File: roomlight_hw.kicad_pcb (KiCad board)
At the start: 2 copper layers, 47.4 x 41.3 mm, 68 parts, among them J1 24V_Conn, J2 LOADs, J3 UART2, J4 DATAs, J5 Touch_SW, J6 SWD, Q1 IRF8734, Q2 IRF8734, Q3 IRF8734, U1 INA180A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

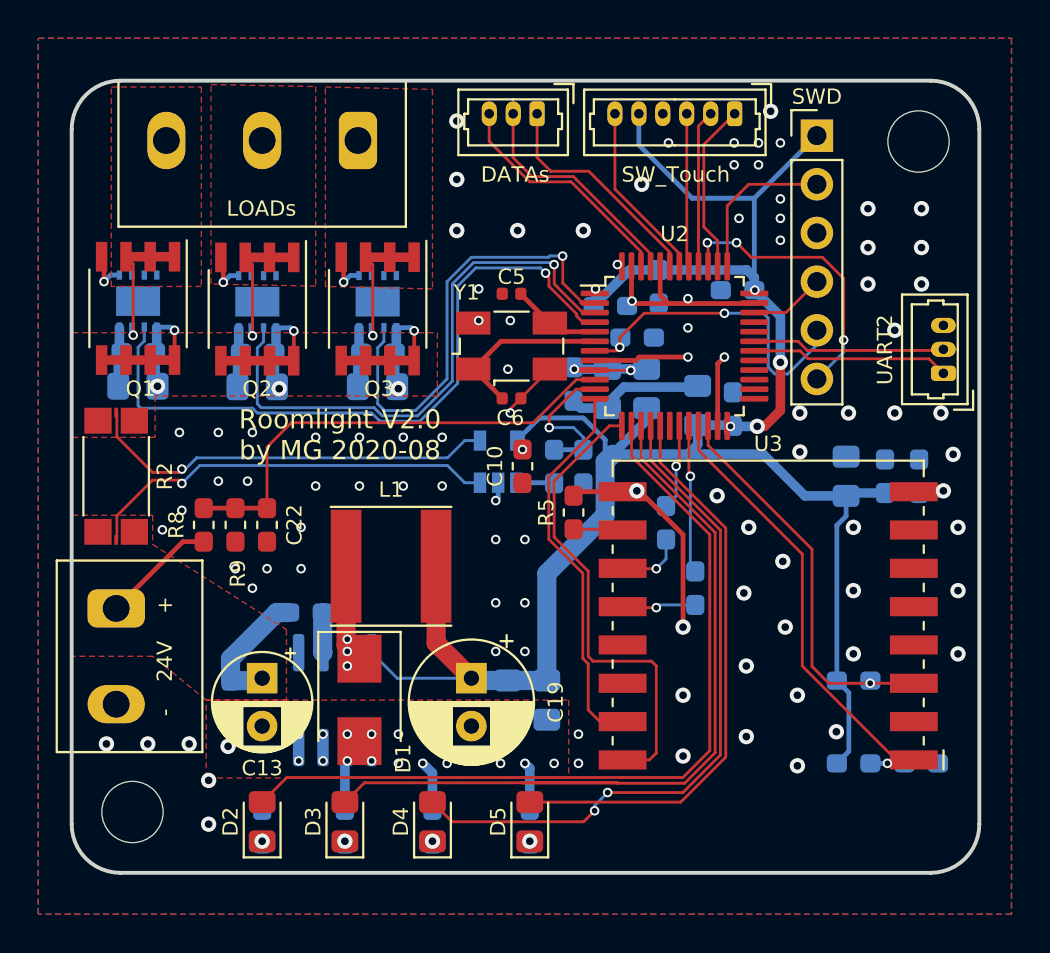
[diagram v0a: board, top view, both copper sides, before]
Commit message: Improve UART connection and a lot of ground planes
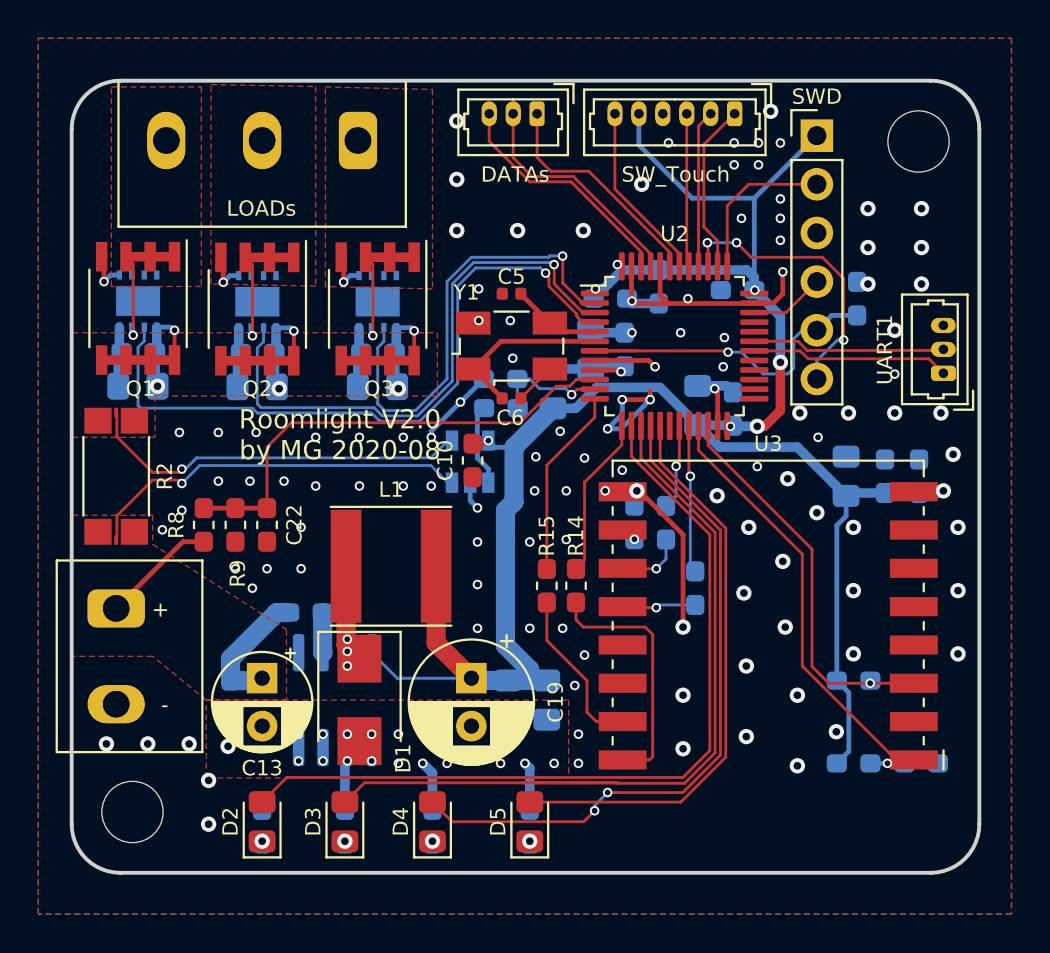
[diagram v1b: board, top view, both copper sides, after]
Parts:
- added R14: R, Resistor_SMD:R_0603_1608Metric_Pad1.05x0.95mm_HandSolder, F.Cu at (76.3, 120.0)
- added R15: R, Resistor_SMD:R_0603_1608Metric_Pad1.05x0.95mm_HandSolder, F.Cu at (74.8, 120.0)
- R5: moved to B.Cu
- moved C9 11.7 mm to (91.0, 105.0), turned to 90 degrees
- moved C3 6.29 mm to (72.4, 109.2), turned to 0 degrees
- moved FB1 4.89 mm to (75.1, 109.7)
- moved R1 4.13 mm to (72.4, 110.7), turned to 0 degrees
- moved C11 3.22 mm to (78.9, 107.7), turned to 90 degrees
- moved R5 3.22 mm to (79.4, 116.7)
- moved C10 2.62 mm to (70.9, 113.5)
- moved C12 2.22 mm to (77.1, 107.7), turned to 90 degrees
- moved U1 1.46 mm to (70.8, 113.5)
- moved C7 0.38 mm to (78.1, 105.0)
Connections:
- U3 pad 15: /UART2_TX -> Net-(R15-Pad2)
- U3 pad 16: /UART2_RX -> Net-(R14-Pad2)
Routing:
- net /UART2_RX: track 24.8 -> 8.46 mm
- net Net-(R14-Pad2): track 0.00 -> 13.2 mm
- net /UART2_TX: track 20.5 -> 9.92 mm
- net Net-(R15-Pad2): track 0.00 -> 8.66 mm
- net GND: track 59.4 -> 65.8 mm, vias 112 -> 134
- net +3V3: track 120.7 -> 117.8 mm
- net Net-(R1-Pad1): track 2.00 -> 4.28 mm
- net Net-(R5-Pad1): track 2.58 -> 0.81 mm, vias 0 -> 1
- net /CURRENT_ADC: track 7.72 -> 6.03 mm
- net /IN+: track 21.8 -> 20.4 mm
- net /IN-: track 21.7 -> 20.2 mm
- net Net-(C11-Pad1): track 6.79 -> 5.58 mm, vias 2 -> 1
- net /~RST: track 17.5 -> 18.5 mm, vias 2 -> 1

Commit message: Update to KiCad 6
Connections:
- net /~RST renamed /~{RST}
- C1 pad 1: +3V3 -> (no net)
- C10 pad 2: +3V3 -> +3.3V
- C16 pad 1: +3V3 -> +3.3V
- C17 pad 1: +3V3 -> +3.3V
- C18 pad 1: +3V3 -> +3.3V
- C19 pad 1: +3V3 -> +3.3V
- C2 pad 1: +3V3 -> +3.3V
- C20 pad 1: +3V3 -> +3.3V
- C21 pad 1: +3V3 -> +3.3V
- C4 pad 1: +3V3 -> +3.3V
- C7 pad 1: +3V3 -> +3.3V
- C8 pad 1: +3V3 -> +3.3V
- FB1 pad 1: +3V3 -> +3.3V
- J5 pad 5: +3V3 -> +3.3V
- J6 pad 1: +3V3 -> +3.3V
- L1 pad 2: +3V3 -> +3.3V
- R3 pad 1: +3V3 -> +3.3V
- R4 pad 1: +3V3 -> +3.3V
- U1 pad 5: +3V3 -> +3.3V
- U2 pad 1: +3V3 -> +3.3V
- U2 pad 24: +3V3 -> +3.3V
- U2 pad 36: +3V3 -> +3.3V
- U2 pad 48: +3V3 -> +3.3V
- U3 pad 8: +3V3 -> +3.3V
- U4 pad 4: +3V3 -> +3.3V
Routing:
- net +3V3: track 117.8 -> 0.00 mm, vias 8 -> 0
- net +3.3V: track 0.00 -> 117.8 mm, vias 0 -> 8
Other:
- net class Default removed
